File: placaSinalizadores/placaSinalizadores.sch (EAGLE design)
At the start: 10 parts

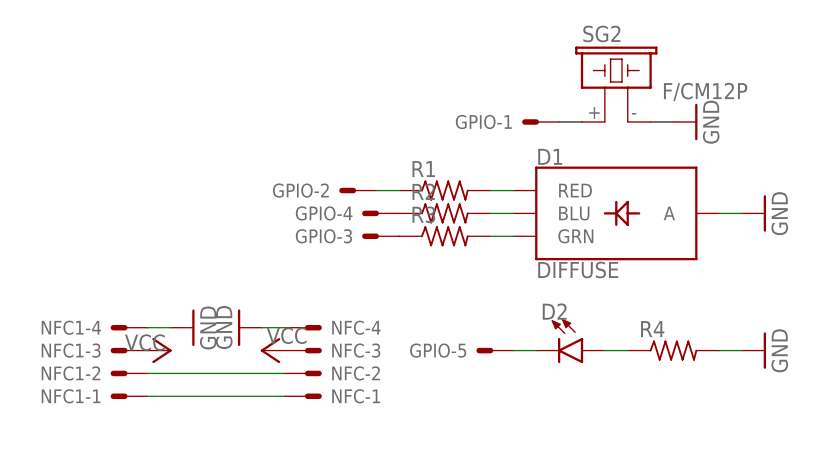
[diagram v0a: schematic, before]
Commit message: placa de sinalização V2
placa com conectores para o reset adicionados e correção do erro para o led rgb
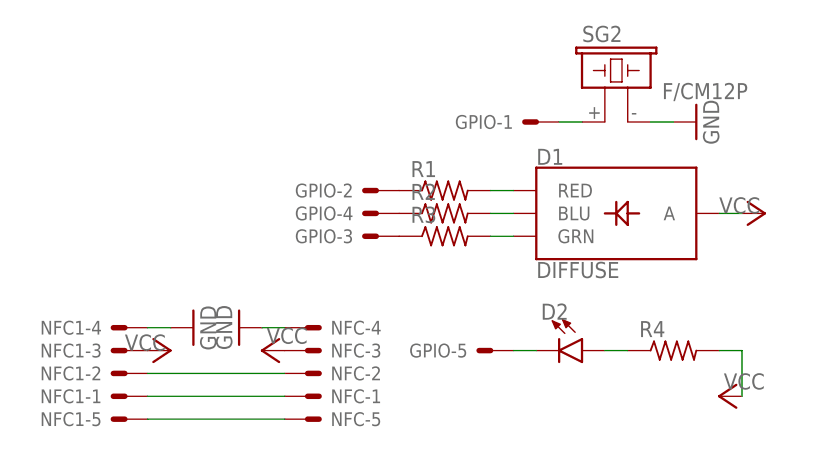
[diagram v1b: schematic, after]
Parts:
- NFC, NFC1: value JST-XH-04-PIN-LONG-PAD -> JST-XH-05-PIN-LONG-PAD; device jst-xh-ornan:JST-XH-04-PIN-LONG-PAD -> jst-xh-ornan:JST-XH-05-PIN-LONG-PAD
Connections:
- new net N$12: NFC-5.S, NFC1-5.S
- net GND: no longer D1.A, R4.2
- net VCC: now also D1.A, R4.2
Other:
- moved on the sheet: GPIO-2
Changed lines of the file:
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@@
 <layer number="18" name="Vias" color="2" fill="1" visible="no" active="no"/>
 <layer number="19" name="Unrouted" color="6" fill="1" visible="no" active="no"/>
-<layer number="20" name="Dimension" color="15" fill="1" visible="no" active="no"/>
+<layer number="20" name="Dimension" color="24" fill="1" visible="no" active="no"/>
 <layer number="21" name="tPlace" color="7" fill="1" visible="no" active="no"/>
 <layer number="22" name="bPlace" color="7" fill="1" visible="no" active="no"/>
@@
 <layer number="49" name="Reference" color="7" fill="1" visible="no" active="no"/>
 <layer number="50" name="dxf" color="7" fill="1" visible="no" active="no"/>
-<layer number="51" name="tDocu" color="6" fill="1" visible="no" active="no"/>
+<layer number="51" name="tDocu" color="7" fill="1" visible="no" active="no"/>
 <layer number="52" name="bDocu" color="7" fill="1" visible="no" active="no"/>
 <layer number="53" name="tGND_GNDA" color="7" fill="9" visible="no" active="no"/>
@@
 <part name="R4" library="rcl-ornan" deviceset="R-US_" device="0204/7" package3d_urn="urn:adsk.eagle:package:23498/2"/>
 <part name="GPIO" library="jst-xh-ornan" deviceset="JST-XH-05-PIN" device="-LONG-PAD" value=""/>
-<part name="NFC" library="jst-xh-ornan" deviceset="JST-XH-04-PIN" device="-LONG-PAD" value=""/>
+<part name="NFC" library="jst-xh-ornan" deviceset="JST-XH-05-PIN" device="-LONG-PAD" value=""/>
 <part name="GND1" library="supply1" library_urn="urn:adsk.eagle:library:371" deviceset="GND" device=""/>
 <part name="P+1" library="supply1" library_urn="urn:adsk.eagle:library:371" deviceset="VCC" device=""/>
-<part name="NFC1" library="jst-xh-ornan" deviceset="JST-XH-04-PIN" device="-LONG-PAD" value=""/>
+<part name="NFC1" library="jst-xh-ornan" deviceset="JST-XH-05-PIN" device="-LONG-PAD" value=""/>
 <part name="GND2" library="supply1" library_urn="urn:adsk.eagle:library:371" deviceset="GND" device=""/>
 <part name="P+2" library="supply1" library_urn="urn:adsk.eagle:library:371" deviceset="VCC" device=""/>
 <part name="GND3" library="supply1" library_urn="urn:adsk.eagle:library:371" deviceset="GND" device=""/>
-<part name="GND4" library="supply1" library_urn="urn:adsk.eagle:library:371" deviceset="GND" device=""/>
-<part name="GND5" library="supply1" library_urn="urn:adsk.eagle:library:371" deviceset="GND" device=""/>
+<part name="P+3" library="supply1" library_urn="urn:adsk.eagle:library:371" deviceset="VCC" device=""/>
+<part name="P+4" library="supply1" library_urn="urn:adsk.eagle:library:371" deviceset="VCC" device=""/>
 </parts>
 <sheets>
@@
 <attribute name="VALUE" x="36.322" y="49.403" size="1.778" layer="96" rot="R180"/>
 </instance>
-<instance part="GPIO" gate="-2" x="15.24" y="43.18" smashed="yes" rot="R180">
-<attribute name="NAME" x="12.7" y="43.942" size="1.524" layer="95" rot="R180"/>
+<instance part="GPIO" gate="-2" x="17.78" y="43.18" smashed="yes" rot="R180">
+<attribute name="NAME" x="15.24" y="43.942" size="1.524" layer="95" rot="R180"/>
 </instance>
 <instance part="GPIO" gate="-3" x="17.78" y="38.1" smashed="yes" rot="R180">
@@
 <attribute name="VALUE" x="55.88" y="48.26" size="1.778" layer="96" rot="R90"/>
 </instance>
-<instance part="GND4" gate="1" x="60.96" y="40.64" smashed="yes" rot="R90">
-<attribute name="VALUE" x="63.5" y="38.1" size="1.778" layer="96" rot="R90"/>
-</instance>
-<instance part="GND5" gate="1" x="60.96" y="25.4" smashed="yes" rot="R90">
-<attribute name="VALUE" x="63.5" y="22.86" size="1.778" layer="96" rot="R90"/>
+<instance part="P+3" gate="VCC" x="60.96" y="40.64" smashed="yes" rot="R270">
+<attribute name="VALUE" x="55.88" y="40.64" size="1.778" layer="96"/>
+</instance>
+<instance part="NFC1" gate="-5" x="-10.16" y="17.78" smashed="yes" rot="R180">
+<attribute name="NAME" x="-12.7" y="18.542" size="1.524" layer="95" rot="R180"/>
+</instance>
+<instance part="NFC" gate="-5" x="10.16" y="17.78" smashed="yes">
+<attribute name="NAME" x="12.7" y="17.018" size="1.524" layer="95"/>
+</instance>
+<instance part="P+4" gate="VCC" x="55.88" y="20.32" smashed="yes" rot="R90">
+<attribute name="VALUE" x="60.96" y="22.86" size="1.778" layer="96" rot="R180"/>
 </instance>
 </instances>
@@
 <wire x1="48.26" y1="50.8" x2="50.8" y2="50.8" width="0.1524" layer="91"/>
 </segment>
-<segment>
-<pinref part="D1" gate="G$1" pin="A"/>
-<pinref part="GND4" gate="1" pin="GND"/>
-<wire x1="55.88" y1="40.64" x2="58.42" y2="40.64" width="0.1524" layer="91"/>
-</segment>
-<segment>
-<pinref part="R4" gate="G$1" pin="2"/>
-<pinref part="GND5" gate="1" pin="GND"/>
-<wire x1="55.88" y1="25.4" x2="58.42" y2="25.4" width="0.1524" layer="91"/>
-</segment>
 </net>
 <net name="VCC" class="0">
@@
 <pinref part="NFC1" gate="-3" pin="S"/>
 <pinref part="P+2" gate="VCC" pin="VCC"/>
+</segment>
+<segment>
+<pinref part="D1" gate="G$1" pin="A"/>
+<wire x1="55.88" y1="40.64" x2="58.42" y2="40.64" width="0.1524" layer="91"/>
+<pinref part="P+3" gate="VCC" pin="VCC"/>
+</segment>
+<segment>
+<pinref part="R4" gate="G$1" pin="2"/>
+<wire x1="55.88" y1="25.4" x2="58.42" y2="25.4" width="0.1524" layer="91"/>
+<pinref part="P+4" gate="VCC" pin="VCC"/>
+<wire x1="58.42" y1="25.4" x2="58.42" y2="20.32" width="0.1524" layer="91"/>
 </segment>
 </net>
@@
 <pinref part="R1" gate="G$1" pin="1"/>
 <pinref part="GPIO" gate="-2" pin="S"/>
-<wire x1="17.78" y1="43.18" x2="20.32" y2="43.18" width="0.1524" layer="91"/>
 </segment>
 </net>
@@
 </segment>
 </net>
+<net name="N$12" class="0">
+<segment>
+<pinref part="NFC1" gate="-5" pin="S"/>
+<pinref part="NFC" gate="-5" pin="S"/>
+<wire x1="-7.62" y1="17.78" x2="7.62" y2="17.78" width="0.1524" layer="91"/>
+</segment>
+</net>
